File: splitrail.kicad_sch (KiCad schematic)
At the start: 1 part, among them U29 LTC3260xMSE

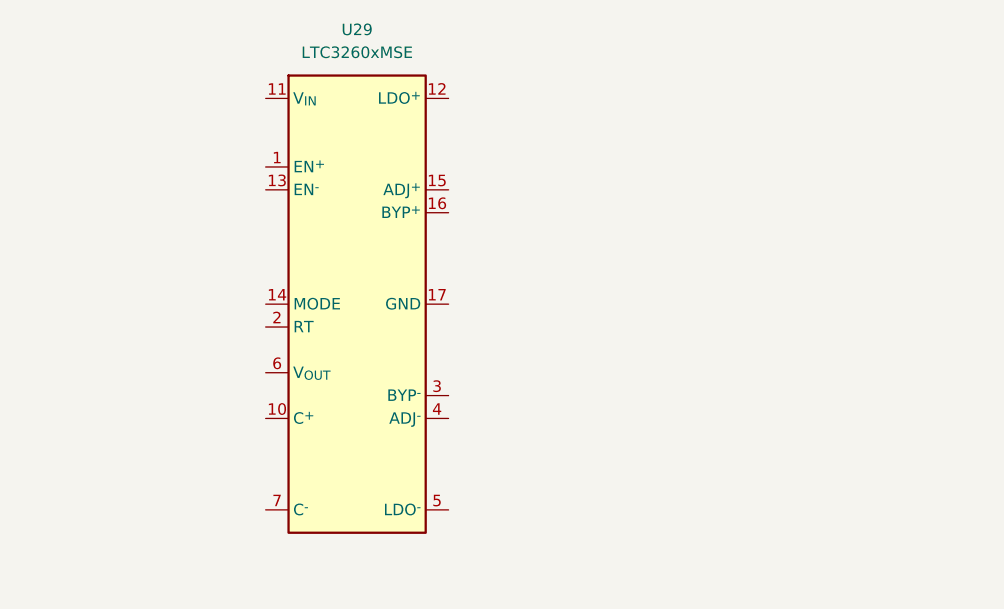
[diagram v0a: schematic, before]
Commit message: Add VVA Bias generator
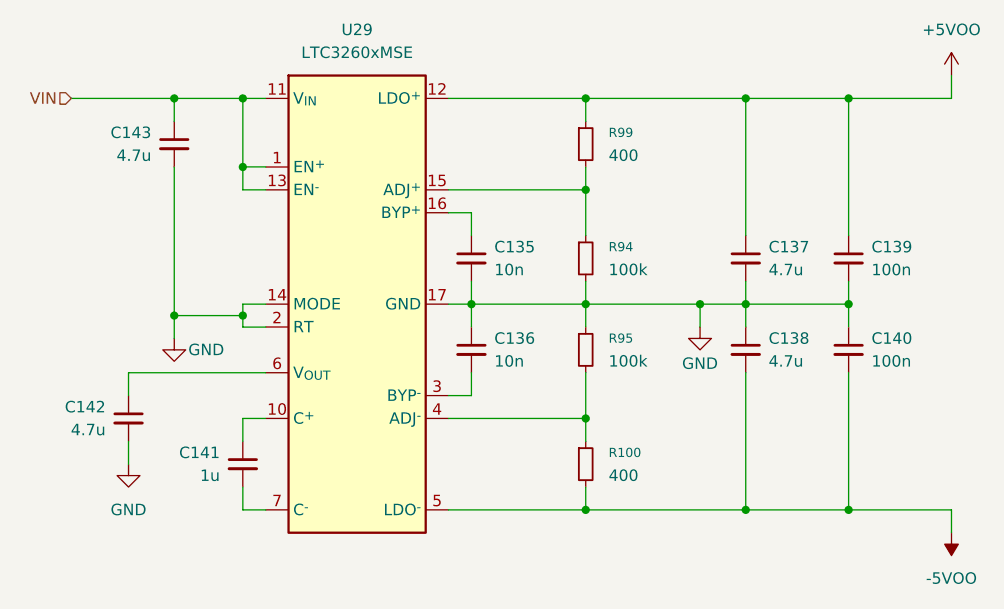
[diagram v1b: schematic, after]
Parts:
- added C135, C136: 10n, symbol Device:C_Small
- added C137, C138, C142, C143: 4.7u, symbol Device:C_Small
- added C139, C140: 100n, symbol Device:C_Small
- added C141: 1u, symbol Device:C_Small
- added R100, R99: 400, symbol Device:R_Small
- added R94, R95: 100k, symbol Device:R_Small
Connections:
- net VIN: now reaches U29.1 (EN^{+})
- net VIN: now also U29.11 (V_{IN}), U29.13 (EN^{-}), C143.1
- net at U29.10 (C^{+}): now also C141.1
- net +5VOO: now reaches U29.12 (LDO^{+})
- net +5VOO: now also C137.1, C139.1, R99.1
- net GND: now reaches U29.14 (MODE)
- net GND: now also U29.17 (GND), U29.2 (RT), C135.2, C136.1, C137.2, C138.1, C139.2, C140.1, C142.2, C143.2, R94.2, R95.1
- net at U29.15 (ADJ^{+}): now also R94.1, R99.2
- net at U29.16 (BYP^{+}): now also C135.1
- net at U29.3 (BYP^{-}): now also C136.2
- net at U29.4 (ADJ^{-}): now also R100.1, R95.2
- net -5VOO: now reaches U29.5 (LDO^{-})
- net -5VOO: now also C138.2, C140.2, R100.2
- net at U29.6 (V_{OUT}): now also C142.1
- net at U29.7 (C^{-}): now also C141.2
